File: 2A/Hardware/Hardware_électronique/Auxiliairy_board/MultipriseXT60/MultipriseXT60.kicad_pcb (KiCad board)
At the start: 2 copper layers, 36 x 115 mm, 11 parts, among them J1 Moteur_gauche, J2 Moteur_Droit, J3 Sécurité, J4 Mainboard, J5 Routeur, J6 Batteries

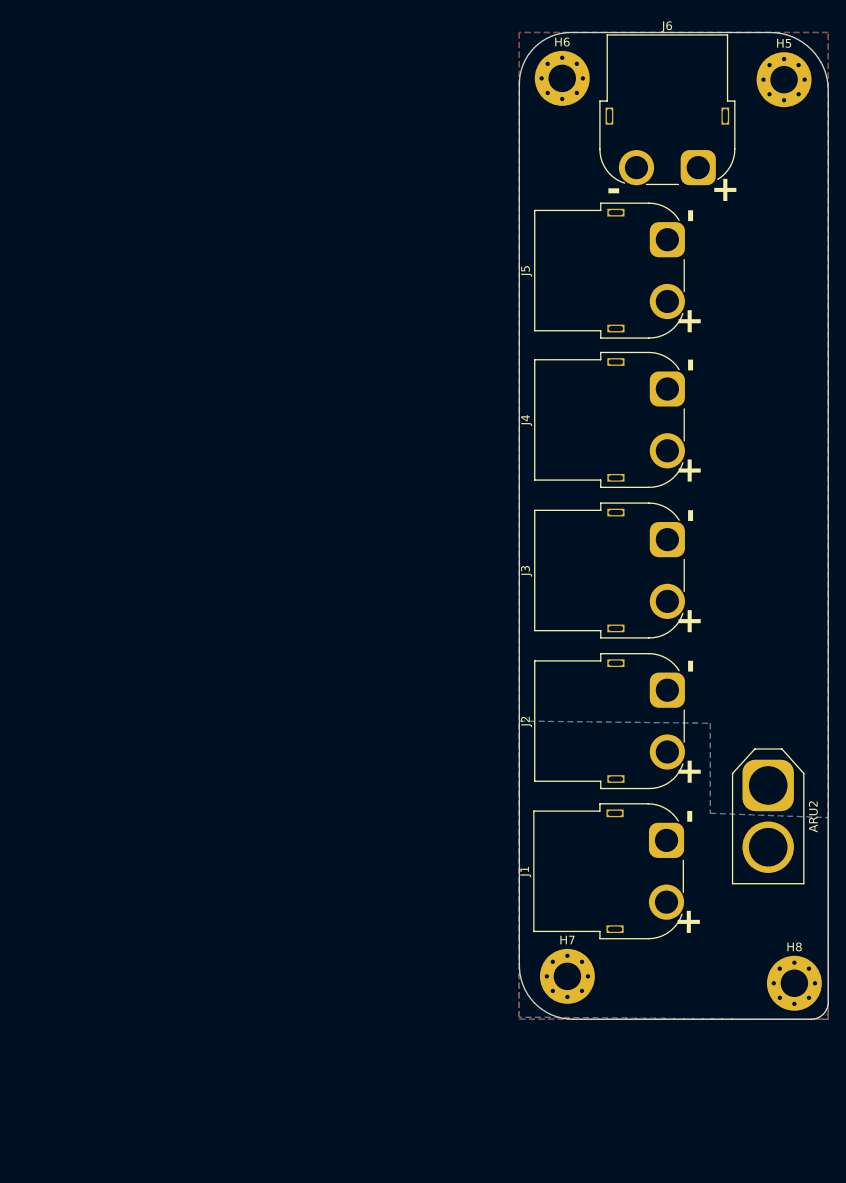
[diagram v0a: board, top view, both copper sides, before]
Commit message: Check Multiprise LF La grille PTN!
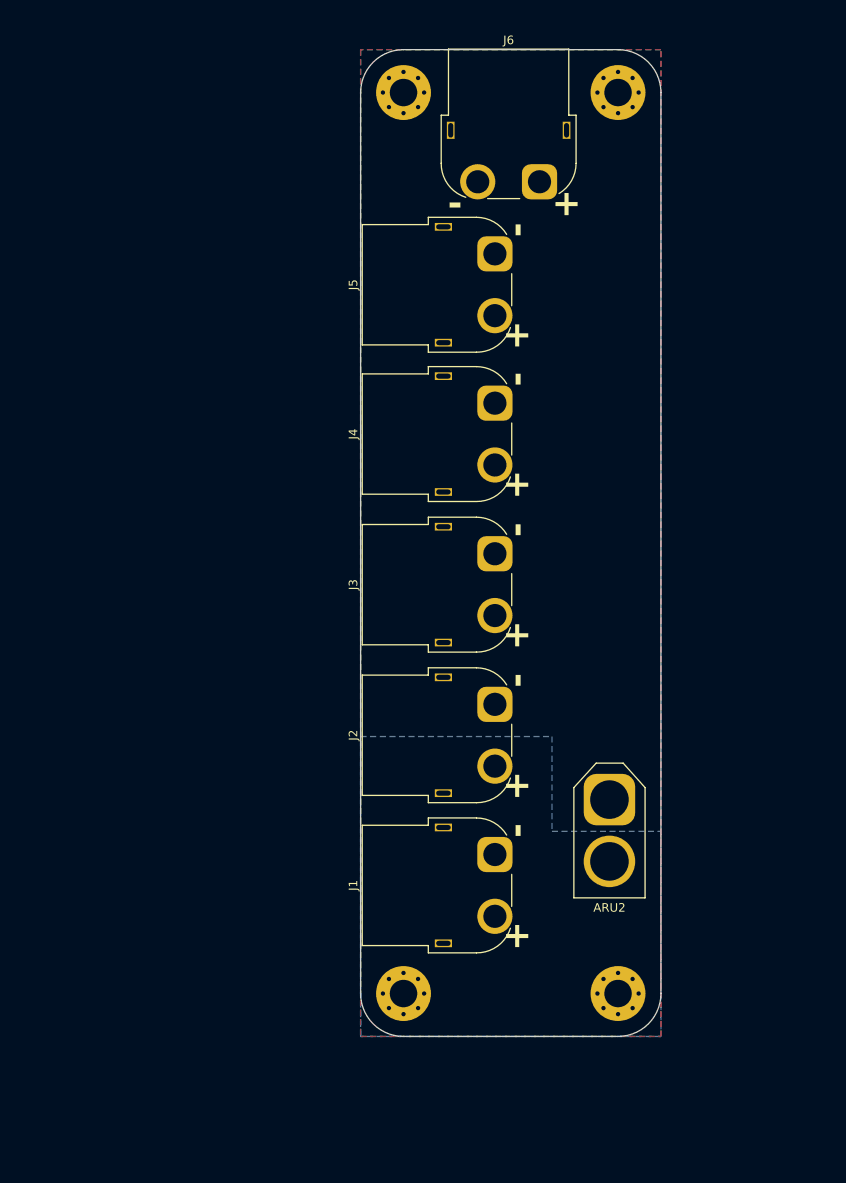
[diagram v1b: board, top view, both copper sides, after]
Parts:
- moved H8 20.6 mm to (125.0, 155.0)
- moved J2 20.2 mm to (110.7, 121.3)
- moved J3 20.2 mm to (110.7, 103.8)
- moved J4 20.2 mm to (110.7, 86.2)
- moved J5 20.2 mm to (110.7, 68.8)
- moved J1 20.1 mm to (110.7, 138.8)
- moved H5 19.4 mm to (125.0, 50.0)
- moved H7 19.2 mm to (100.0, 155.0)
- moved ARU2 18.6 mm to (124.0, 132.4)
- moved H6 18.6 mm to (100.0, 50.0)
- moved J6 18.6 mm to (115.8, 60.4)
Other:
- board size 36 x 115 mm -> 35 x 115 mm
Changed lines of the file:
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@@
 	(footprint "MountingHole:MountingHole_3.2mm_M3_Pad_Via"
 		(layer "F.Cu")
-		(at 144.35 48.5)
+		(at 125 50)
 		(descr "Mounting Hole 3.2mm, M3")
 		(tags "mounting hole 3.2mm m3")
@@
 			(at 0 -4.2 0)
 			(layer "F.SilkS")
+			(hide yes)
 			(effects
 				(font
@@
 	(footprint "Connector_AMASS:AMASS_XT60-F_1x02_P7.20mm_Vertical"
 		(layer "F.Cu")
-		(at 142.5 130.75 -90)
+		(at 124 132.4 -90)
 		(descr "AMASS female XT60, through hole, vertical, https://www.tme.eu/Document/2d152ced3b7a446066e6c419d84bb460/XT60%20SPEC.pdf")
 		(tags "XT60 female vertical")
 		(property "Reference" "ARU2"
-			(at 3.6 -5.3 90)
+			(at 12.6 0 0)
 			(layer "F.SilkS")
 			(effects
@@
 	(footprint "Connector_AMASS:AMASS_XT60PW-F_1x02_P7.20mm_Horizontal"
 		(layer "F.Cu")
-		(at 130.75 102.1 90)
+		(at 110.65 103.75 90)
 		(descr "Connector XT60 Horizontal PCB Female, https://www.tme.eu/en/Document/9b8d0c5eb7094295f3d3112c214d3ade/XT60PW%20SPEC.pdf")
 		(tags "RC Connector XT60")
@@
 	(footprint "Connector_AMASS:AMASS_XT60PW-F_1x02_P7.20mm_Horizontal"
 		(layer "F.Cu")
-		(at 130.65 137.15 90)
+		(at 110.65 138.8 90)
 		(descr "Connector XT60 Horizontal PCB Female, https://www.tme.eu/en/Document/9b8d0c5eb7094295f3d3112c214d3ade/XT60PW%20SPEC.pdf")
 		(tags "RC Connector XT60")
@@
 	(footprint "Connector_AMASS:AMASS_XT60PW-F_1x02_P7.20mm_Horizontal"
 		(layer "F.Cu")
-		(at 130.75 84.55 90)
+		(at 110.65 86.2 90)
 		(descr "Connector XT60 Horizontal PCB Female, https://www.tme.eu/en/Document/9b8d0c5eb7094295f3d3112c214d3ade/XT60PW%20SPEC.pdf")
 		(tags "RC Connector XT60")
@@
 	(footprint "MountingHole:MountingHole_3.2mm_M3_Pad_Via"
 		(layer "F.Cu")
-		(at 119.1 153)
+		(at 100 155)
 		(descr "Mounting Hole 3.2mm, M3")
 		(tags "mounting hole 3.2mm m3")
@@
 			(at 0 -4.2 0)
 			(layer "F.SilkS")
+			(hide yes)
 			(effects
 				(font
@@
 	(footprint "MountingHole:MountingHole_3.2mm_M3_Pad_Via"
 		(layer "F.Cu")
-		(at 118.5 48.35)
+		(at 100 50)
 		(descr "Mounting Hole 3.2mm, M3")
 		(tags "mounting hole 3.2mm m3")
@@
 			(at 0 -4.2 0)
 			(layer "F.SilkS")
+			(hide yes)
 			(effects
 				(font
@@
 	(footprint "Connector_AMASS:AMASS_XT60PW-F_1x02_P7.20mm_Horizontal"
 		(layer "F.Cu")
-		(at 130.75 67.15 90)
+		(at 110.65 68.8 90)
 		(descr "Connector XT60 Horizontal PCB Female, https://www.tme.eu/en/Document/9b8d0c5eb7094295f3d3112c214d3ade/XT60PW%20SPEC.pdf")
 		(tags "RC Connector XT60")
@@
 	(footprint "MountingHole:MountingHole_3.2mm_M3_Pad_Via"
 		(layer "F.Cu")
-		(at 145.552944 153.802944)
+		(at 125 155)
 		(descr "Mounting Hole 3.2mm, M3")
 		(tags "mounting hole 3.2mm m3")
@@
 			(at 0 -4.2 0)
 			(layer "F.SilkS")
+			(hide yes)
 			(effects
 				(font
@@
 	(footprint "Connector_AMASS:AMASS_XT60PW-F_1x02_P7.20mm_Horizontal"
 		(layer "F.Cu")
-		(at 134.35 58.75)
+		(at 115.85 60.4)
 		(descr "Connector XT60 Horizontal PCB Female, https://www.tme.eu/en/Document/9b8d0c5eb7094295f3d3112c214d3ade/XT60PW%20SPEC.pdf")
 		(tags "RC Connector XT60")
@@
 	(footprint "Connector_AMASS:AMASS_XT60PW-F_1x02_P7.20mm_Horizontal"
 		(layer "F.Cu")
-		(at 130.75 119.65 90)
+		(at 110.65 121.3 90)
 		(descr "Connector XT60 Horizontal PCB Female, https://www.tme.eu/en/Document/9b8d0c5eb7094295f3d3112c214d3ade/XT60PW%20SPEC.pdf")
 		(tags "RC Connector XT60")
@@
 	)
 	(gr_arc
-		(start 149.5 156)
-		(mid 148.914214 157.414214)
-		(end 147.5 158)
+		(start 95 50)
+		(mid 96.464466 46.464466)
+		(end 100 45)
 		(stroke
 			(width 0.05)
@@
 		(layer "Edge.Cuts")
 	)
-	(gr_line
-		(start 113.5 49)
-		(end 113.5 151.5)
+	(gr_arc
+		(start 130 155)
+		(mid 128.535534 158.535534)
+		(end 125 160)
 		(stroke
 			(width 0.05)
@@
 		(layer "Edge.Cuts")
 	)
-	(gr_line
-		(start 149.5 156)
-		(end 149.5 49.75)
+	(gr_arc
+		(start 100 160)
+		(mid 96.464466 158.535534)
+		(end 95 155)
 		(stroke
 			(width 0.05)
@@
 	)
 	(gr_line
-		(start 119.5 43)
-		(end 142.75 43)
+		(start 95 50)
+		(end 95 155)
 		(stroke
 			(width 0.05)
@@
 	)
 	(gr_line
-		(start 119.75 158)
-		(end 147.5 158)
+		(start 125 45)
+		(end 100 45)
 		(stroke
 			(width 0.05)
@@
 		(layer "Edge.Cuts")
 	)
-	(gr_arc
-		(start 113.5 49)
-		(mid 115.257359 44.757359)
-		(end 119.5 43)
+	(gr_line
+		(start 100 160)
+		(end 125 160)
 		(stroke
 			(width 0.05)
@@
 		(layer "Edge.Cuts")
 	)
-	(gr_arc
-		(start 119.75 158)
-		(mid 115.24313 156.080199)
-		(end 113.504994 151.5002)
+	(gr_line
+		(start 130 155)
+		(end 130 50)
 		(stroke
 			(width 0.05)
@@
 	)
 	(gr_arc
-		(start 142.75 43)
-		(mid 147.522971 44.977029)
-		(end 149.5 49.75)
+		(start 125 45)
+		(mid 128.535534 46.464466)
+		(end 130 50)
 		(stroke
 			(width 0.05)
@@
 		(polygon
 			(pts
-				(xy 113.5 43) (xy 113.5 158) (xy 149.5 158) (xy 149.5 43)
+				(xy 95 45) (xy 95 160) (xy 130 160) (xy 130 45)
 			)
 		)
@@
 		(polygon
 			(pts
-				(xy 113.5 157.75) (xy 113.5 123.25) (xy 135.75 123.5) (xy 135.75 134) (xy 149.5 134.5) (xy 149.5 158)
-				(xy 141.75 158)
+				(xy 95 160) (xy 95 125.05) (xy 117.3 125.05) (xy 117.3 136.1) (xy 130 136.1) (xy 130 160)
 			)
 		)
@@
 		(polygon
 			(pts
-				(xy 113.5 43) (xy 113.5 158) (xy 149.5 158) (xy 149.5 43)
+				(xy 95 45) (xy 95 160) (xy 130 160) (xy 130 45)
 			)
 		)

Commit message: change on kicad projects, remove errors
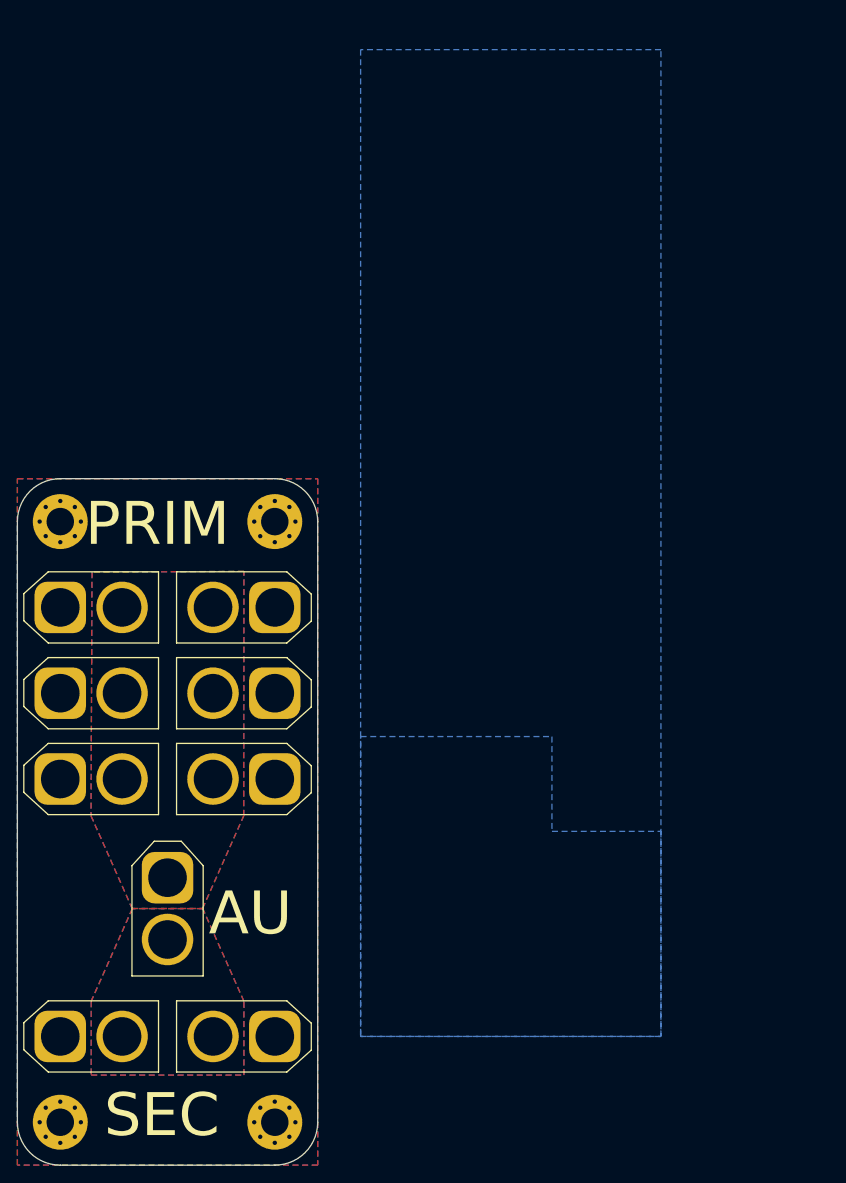
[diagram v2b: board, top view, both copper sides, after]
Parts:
- added J7: Conn_01x02_Pin, Connector_AMASS:AMASS_XT60-F_1x02_P7.20mm_Vertical, F.Cu at (85.0, 110.0)
- added J8: Conn_01x02_Pin, Connector_AMASS:AMASS_XT60-F_1x02_P7.20mm_Vertical, F.Cu at (60.0, 110.0)
- J1: value Moteur_gauche -> Conn_01x02_Pin; footprint Connector_AMASS:AMASS_XT60PW-F_1x02_P7.20mm_Horizontal -> Connector_AMASS:AMASS_XT60-F_1x02_P7.20mm_Vertical
- J2: value Moteur_Droit -> Conn_01x02_Pin; footprint Connector_AMASS:AMASS_XT60PW-F_1x02_P7.20mm_Horizontal -> Connector_AMASS:AMASS_XT60-F_1x02_P7.20mm_Vertical
- J3: value Sécurité -> Conn_01x02_Pin; footprint Connector_AMASS:AMASS_XT60PW-F_1x02_P7.20mm_Horizontal -> Connector_AMASS:AMASS_XT60-F_1x02_P7.20mm_Vertical
- J4: value Mainboard -> Conn_01x02_Pin; footprint Connector_AMASS:AMASS_XT60PW-F_1x02_P7.20mm_Horizontal -> Connector_AMASS:AMASS_XT60-F_1x02_P7.20mm_Vertical
- J5: value Routeur -> Conn_01x02_Pin; footprint Connector_AMASS:AMASS_XT60PW-F_1x02_P7.20mm_Horizontal -> Connector_AMASS:AMASS_XT60-F_1x02_P7.20mm_Vertical
- J6: value Batteries -> Conn_01x02_Pin; footprint Connector_AMASS:AMASS_XT60PW-F_1x02_P7.20mm_Horizontal -> Connector_AMASS:AMASS_XT60-F_1x02_P7.20mm_Vertical
- moved J6 89.2 mm to (60.0, 130.0)
- moved J5 72.0 mm to (60.0, 120.0), turned to 0 degrees
- moved H5 64.0 mm to (85.0, 100.0)
- moved H6 64.0 mm to (60.0, 100.0)
- moved J2 63.7 mm to (60.0, 160.0), turned to 0 degrees
- moved ARU2 52.3 mm to (72.5, 141.5)
- moved H7 42.7 mm to (60.0, 170.0)
- moved H8 42.7 mm to (85.0, 170.0)
- moved J4 42.4 mm to (85.0, 120.0), turned to 180 degrees
- moved J3 36.7 mm to (85.0, 130.0), turned to 180 degrees
- moved J1 33.3 mm to (85.0, 160.0), turned to 180 degrees
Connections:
- J6 pad 1: BAT+ -> GND
- J6 pad 2: GND -> BAT+
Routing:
- added copper zone on F.Cu, net BAT+
- added copper zone on B.Cu, net GND
- added copper zone on F.Cu, net SEC
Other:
- board size 35 x 115 mm -> 35 x 80 mm
- board text added: "AU"
- board text added: "PRIM"
- board text added: "SEC"
